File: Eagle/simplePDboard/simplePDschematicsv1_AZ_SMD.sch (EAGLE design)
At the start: 14 parts, among them IC1 OP27Z

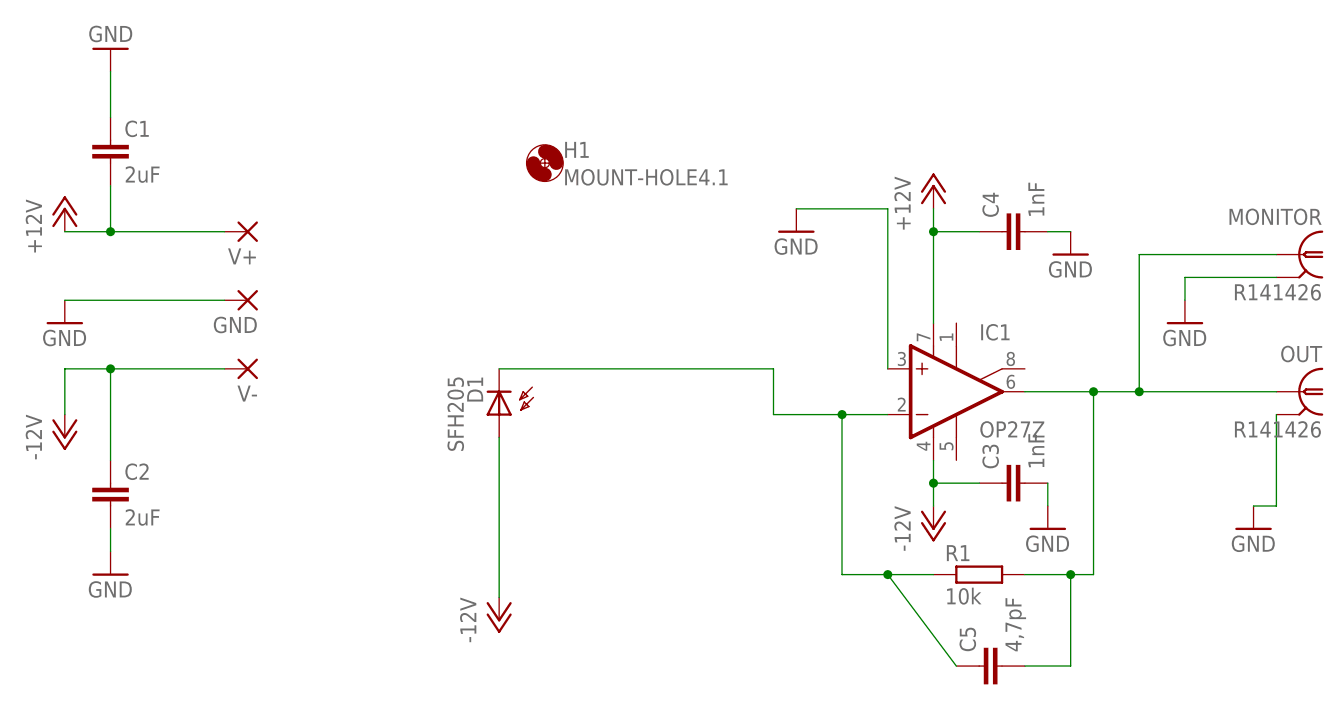
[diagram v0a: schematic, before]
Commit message: A very simple Transimpedence design. The version we finally test is the version AZ_SMD
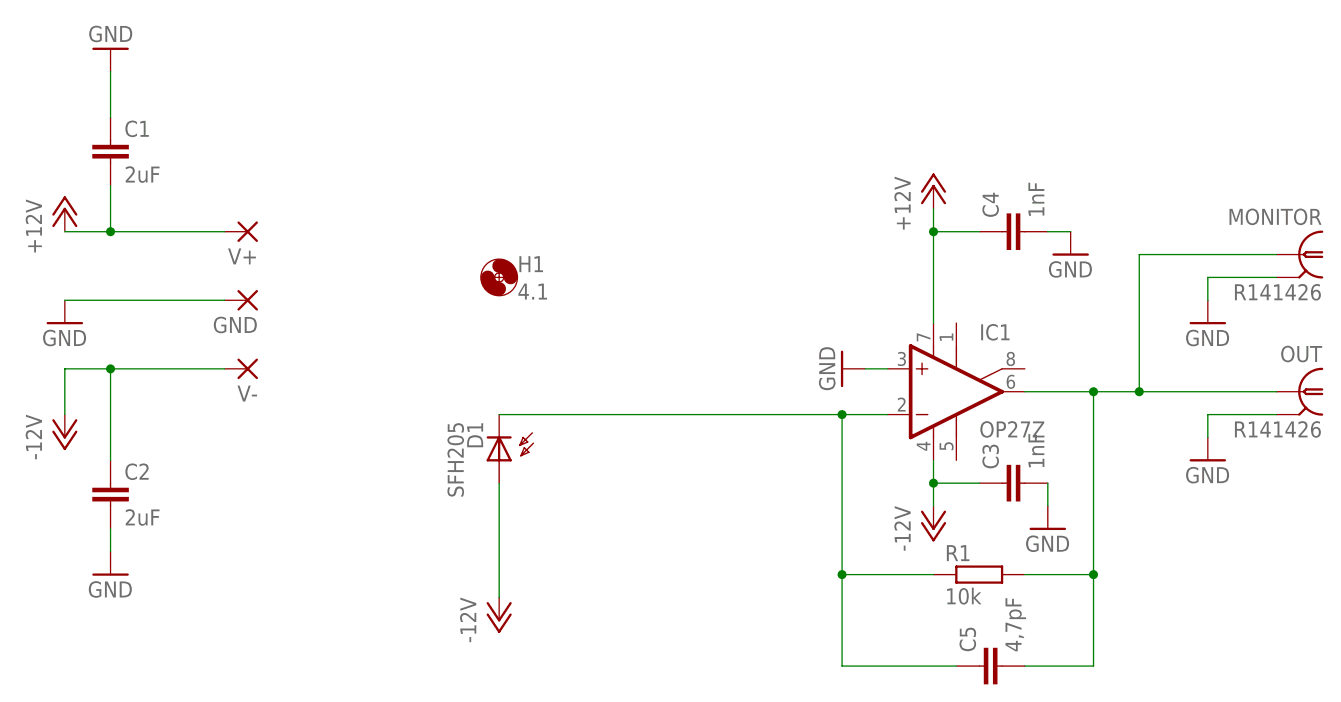
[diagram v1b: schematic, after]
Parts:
- H1: value MOUNT-HOLE4.1 -> 4.1
- R1: device resistor:R-EU_0207/10 -> resistor:R-EU_M1206
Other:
- moved on the sheet: D1, H1
